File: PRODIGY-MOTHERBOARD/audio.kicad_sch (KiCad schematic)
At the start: 5 parts, among them J28 AudioJack4, U24 CS43L21, U8 Si4460, U9 LM386

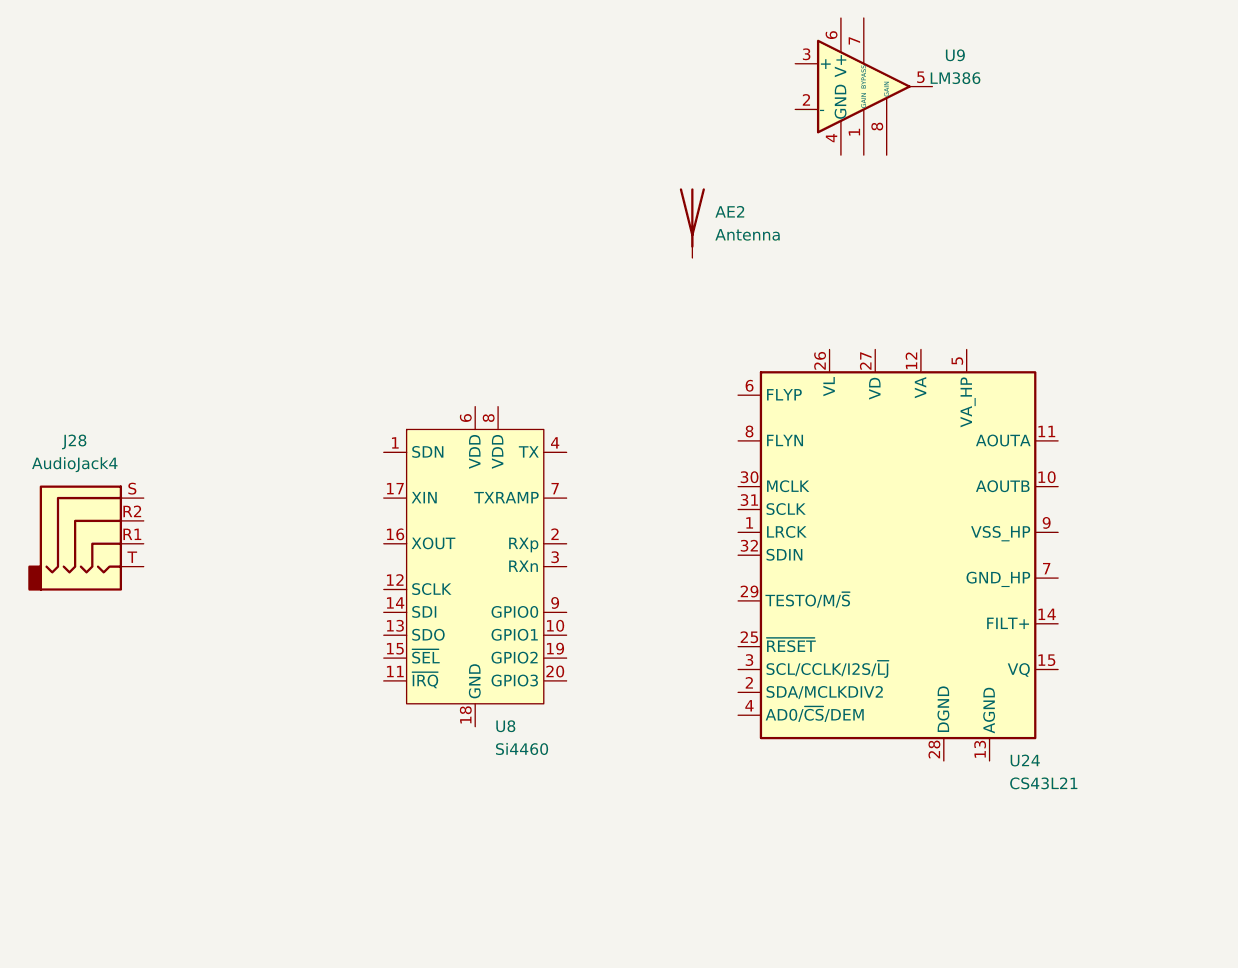
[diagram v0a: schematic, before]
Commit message: Added proper debounce filter elements to buttons.
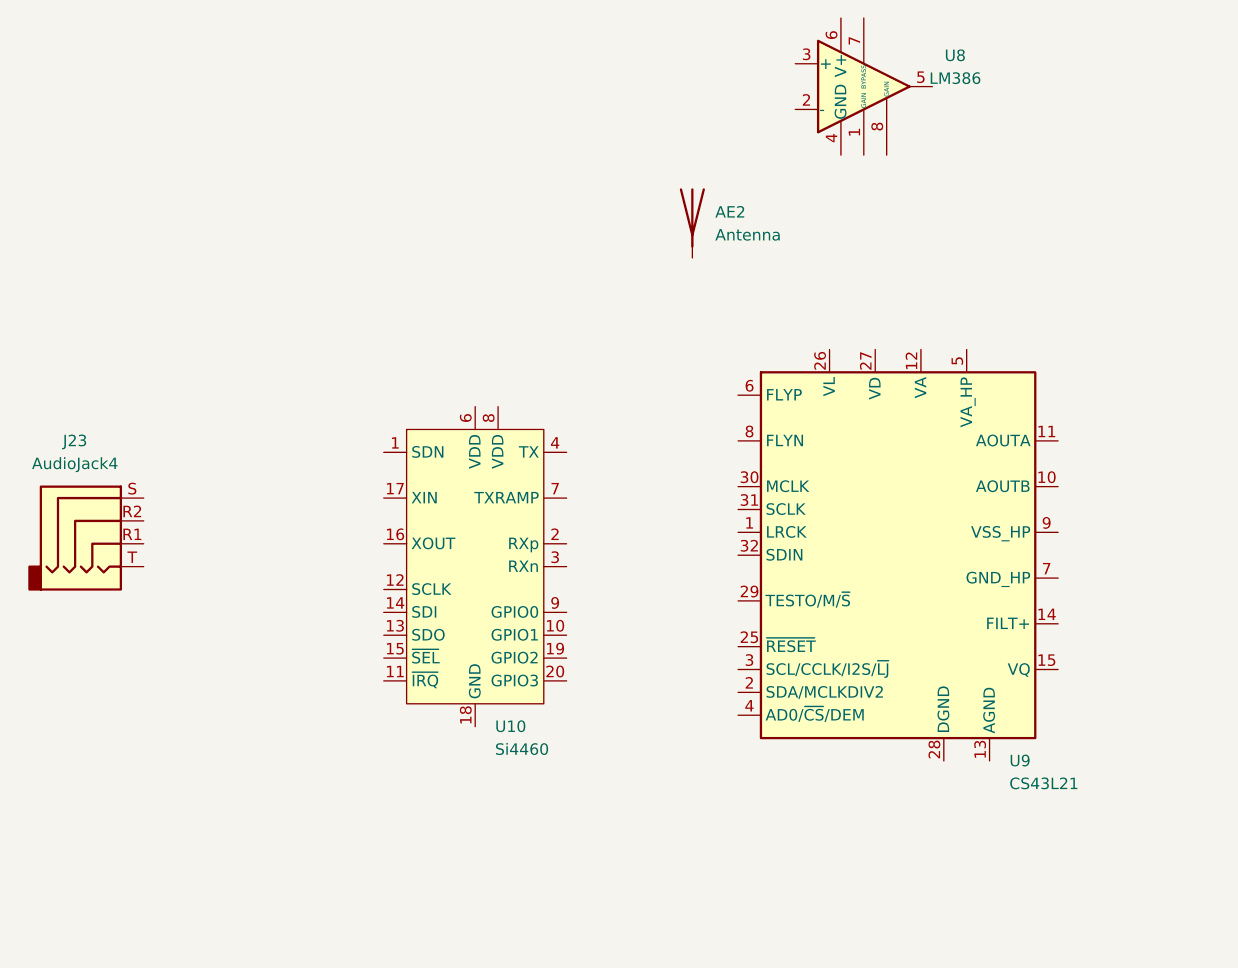
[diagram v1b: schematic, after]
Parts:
- renumbered J28 to J23, U8 to U10, U9 to U8, U24 to U9
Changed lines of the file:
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@@
 		(dnp no)
 		(fields_autoplaced yes)
-		(property "Reference" "U8"
+		(property "Reference" "U10"
 			(at 150.7841 115.57 0)
 			(effects
@@
 			(project "PRODIGY-MOTHERBOARD"
 				(path "/f1c25860-8989-4190-bd24-2491d23ca7d9/e2913798-f444-47a6-8b64-53020d7d816b/beae7986-1156-4b71-ad5e-6c6ef7c2c7f1"
-					(reference "U8")
+					(reference "U10")
 					(unit 1)
 				)
@@
 		(dnp no)
 		(fields_autoplaced yes)
-		(property "Reference" "U24"
+		(property "Reference" "U9"
 			(at 207.9341 119.38 0)
 			(effects
@@
 			(project "PRODIGY-MOTHERBOARD"
 				(path "/f1c25860-8989-4190-bd24-2491d23ca7d9/e2913798-f444-47a6-8b64-53020d7d816b/beae7986-1156-4b71-ad5e-6c6ef7c2c7f1"
-					(reference "U24")
+					(reference "U9")
 					(unit 1)
 				)
@@
 		(dnp no)
 		(fields_autoplaced yes)
-		(property "Reference" "J28"
+		(property "Reference" "J23"
 			(at 104.14 83.82 0)
 			(effects
@@
 			(project "PRODIGY-MOTHERBOARD"
 				(path "/f1c25860-8989-4190-bd24-2491d23ca7d9/e2913798-f444-47a6-8b64-53020d7d816b/beae7986-1156-4b71-ad5e-6c6ef7c2c7f1"
-					(reference "J28")
+					(reference "J23")
 					(unit 1)
 				)
@@
 		(dnp no)
 		(fields_autoplaced yes)
-		(property "Reference" "U9"
+		(property "Reference" "U8"
 			(at 201.93 41.0211 0)
 			(effects
@@
 			(project "PRODIGY-MOTHERBOARD"
 				(path "/f1c25860-8989-4190-bd24-2491d23ca7d9/e2913798-f444-47a6-8b64-53020d7d816b/beae7986-1156-4b71-ad5e-6c6ef7c2c7f1"
-					(reference "U9")
+					(reference "U8")
 					(unit 1)
 				)

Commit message: Submitted V0 for evaluation. Avaiting feedback.
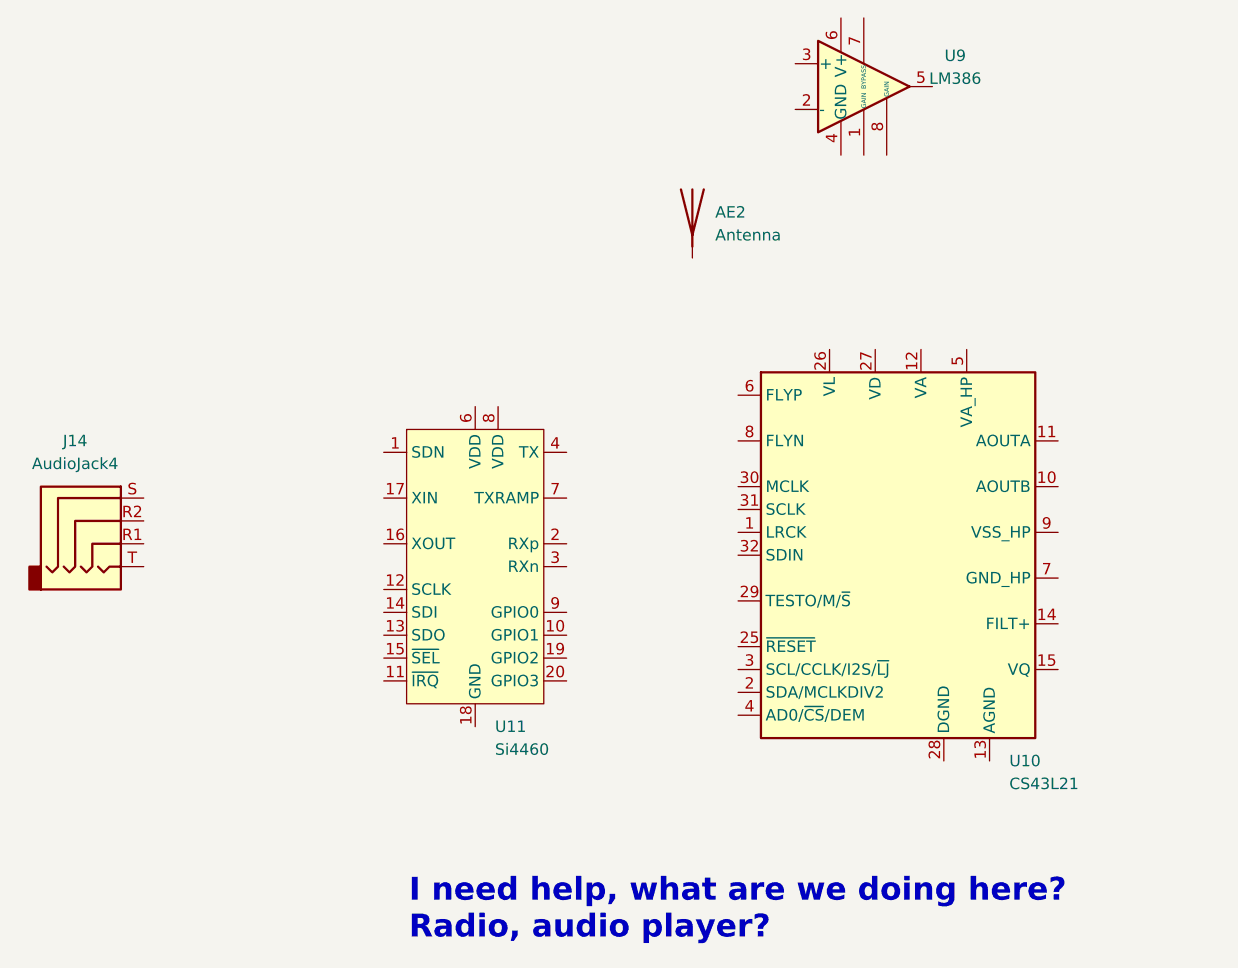
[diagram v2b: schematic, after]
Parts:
- renumbered J23 to J14, U9 to U10, U10 to U11, U8 to U9
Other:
- note added: "I need help, what are we doing here? Radio, audio player?"
